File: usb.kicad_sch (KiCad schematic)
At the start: 1 part, among them U2 RTL8211FD-CG

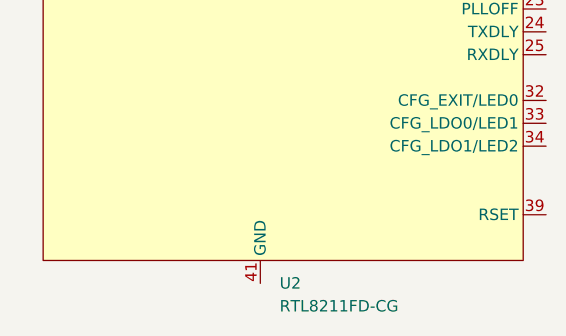
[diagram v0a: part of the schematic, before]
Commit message: Started power circuitry and added more custom schematic symbols
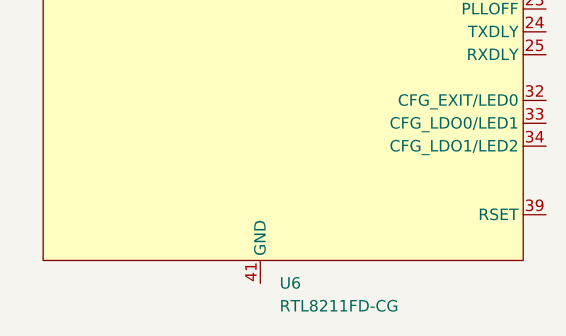
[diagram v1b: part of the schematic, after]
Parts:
- renumbered U2 to U6
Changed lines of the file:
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@@
 		(dnp no)
 		(fields_autoplaced yes)
-		(property "Reference" "U2"
+		(property "Reference" "U6"
 			(at 111.3633 177.8 0)
 			(effects
@@
 		(pin "25"
 		)
+		(instances
+			(project "Leonhart"
+				(path "/b43b7bca-e50d-42ec-8ff0-e0016dfefe0a/0f49ee45-e999-4887-835b-49de9bc4f6ff"
+					(reference "U7")
+					(unit 1)
+				)
+				(path "/b43b7bca-e50d-42ec-8ff0-e0016dfefe0a/5ce8c427-fcc7-46d6-9710-77fc43565e4a"
+					(reference "U8")
+					(unit 1)
+				)
+				(path "/b43b7bca-e50d-42ec-8ff0-e0016dfefe0a/e2459660-886d-4599-a9e6-b9bb7931d0e6"
+					(reference "U6")
+					(unit 1)
+				)
+			)
+		)
 	)

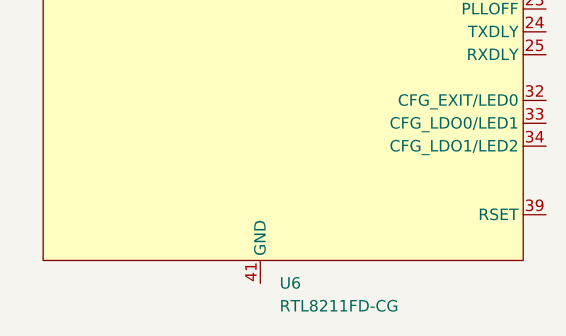
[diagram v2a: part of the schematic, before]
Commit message: Fixed schematic symbol errors
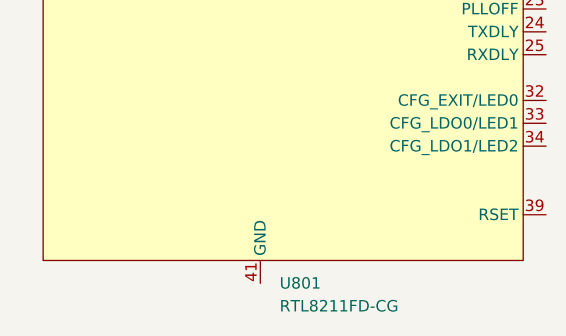
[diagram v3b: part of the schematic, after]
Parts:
- removed U6: RTL8211FD-CG, symbol SoftServicesSymbolLibrary:RTL8211FD-CG
- added U801: RTL8211FD-CG, symbol SoftServicesSymbolLibrary:RTL8211FD-CG
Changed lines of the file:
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@@
 		(dnp no)
 		(fields_autoplaced yes)
-		(property "Reference" "U6"
+		(property "Reference" "U801"
 			(at 111.3633 177.8 0)
 			(effects
@@
 			(project "Leonhart"
 				(path "/b43b7bca-e50d-42ec-8ff0-e0016dfefe0a/e2459660-886d-4599-a9e6-b9bb7931d0e6"
-					(reference "U6")
+					(reference "U801")
 					(unit 1)
 				)

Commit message: Added some net labels and schematic routing
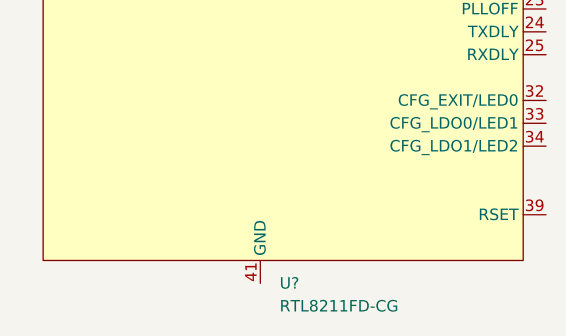
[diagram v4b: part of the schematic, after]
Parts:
- renumbered U801 to U?
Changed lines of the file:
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@@
 		(dnp no)
 		(fields_autoplaced yes)
-		(property "Reference" "U801"
+		(property "Reference" "U?"
 			(at 111.3633 177.8 0)
 			(effects
@@
 			(project "Leonhart"
 				(path "/b43b7bca-e50d-42ec-8ff0-e0016dfefe0a/e2459660-886d-4599-a9e6-b9bb7931d0e6"
-					(reference "U801")
+					(reference "U?")
 					(unit 1)
 				)

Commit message: Worked on schematic for DDR4 memory
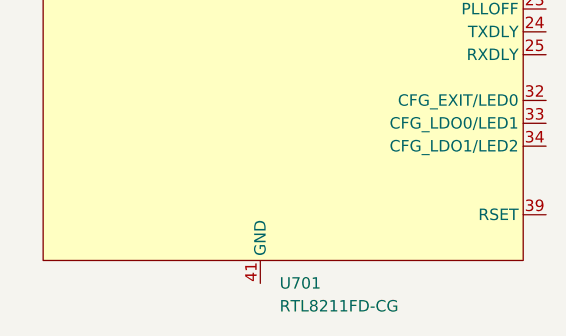
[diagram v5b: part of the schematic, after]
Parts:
- gave numbers to parts that had none: 1
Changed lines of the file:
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@@
 		(dnp no)
 		(fields_autoplaced yes)
-		(property "Reference" "U?"
+		(property "Reference" "U701"
 			(at 111.3633 177.8 0)
 			(effects
@@
 			(project "Leonhart"
 				(path "/b43b7bca-e50d-42ec-8ff0-e0016dfefe0a/e2459660-886d-4599-a9e6-b9bb7931d0e6"
-					(reference "U?")
+					(reference "U701")
 					(unit 1)
 				)

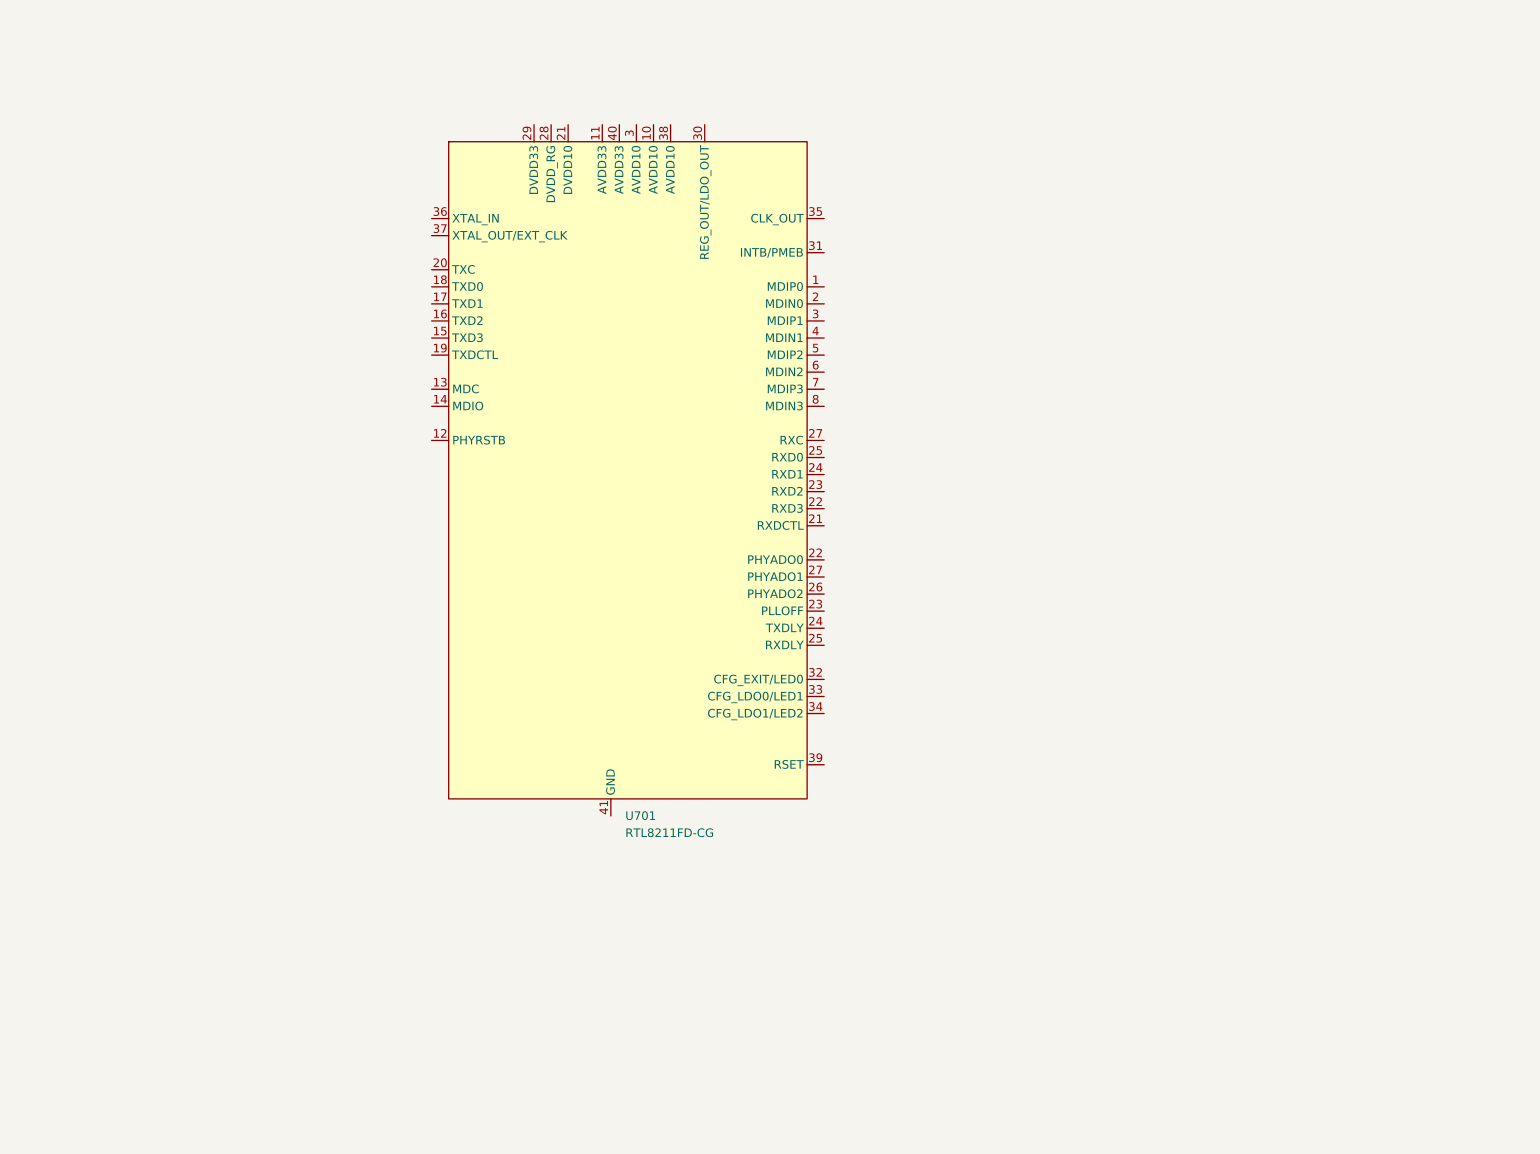
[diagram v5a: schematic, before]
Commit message: Added USB A and USB C to the schematic
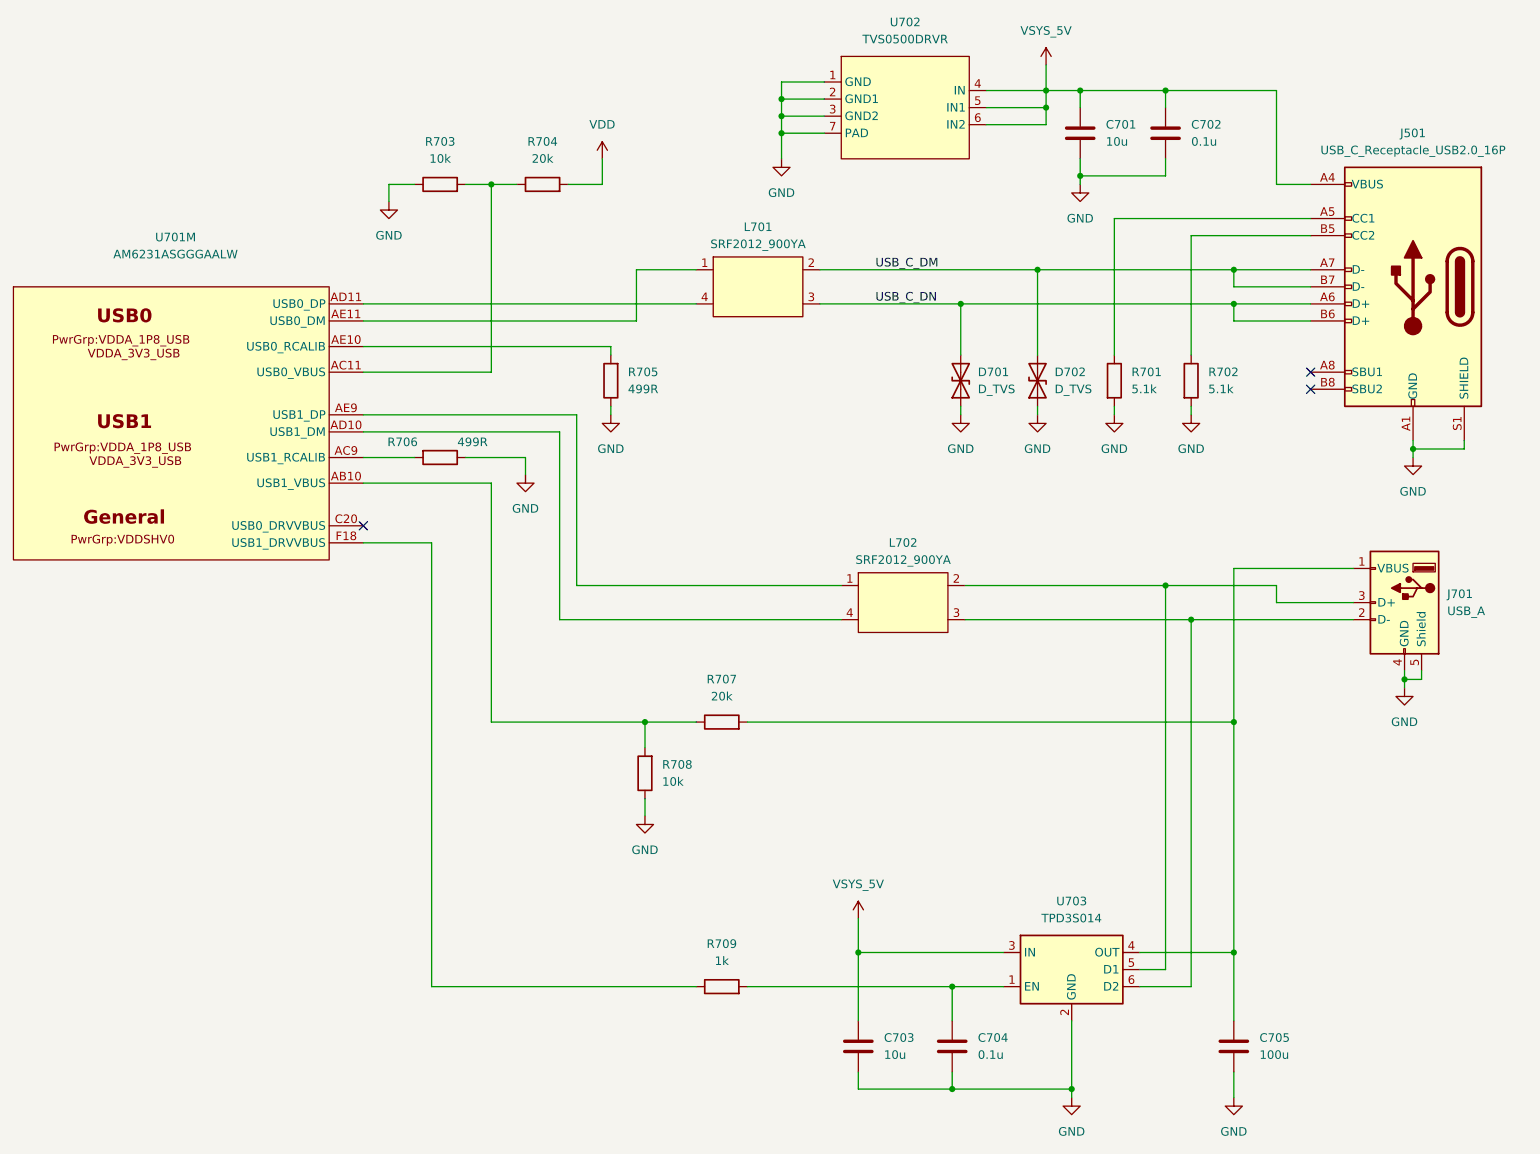
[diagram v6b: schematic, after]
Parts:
- removed U701: RTL8211FD-CG, symbol SoftServicesSymbolLibrary:RTL8211FD-CG
- added C701, C703: 10u, symbol Device:C
- added C702, C704: 0.1u, symbol Device:C
- added C705: 100u, symbol Device:C
- added D701, D702: D_TVS, symbol Device:D_TVS
- added J501: USB_C_Receptacle_USB2.0_16P, symbol Connector:USB_C_Receptacle_USB2.0_16P
- added J701: USB_A, symbol Connector:USB_A
- added L701, L702: SRF2012_900YA, symbol SoftServicesSymbolLibrary:SRF2012_900YA
- added R701, R702: 5.1k, symbol Device:R
- added R703, R708: 10k, symbol Device:R
- added R704, R707: 20k, symbol Device:R
- added R705, R706: 499R, symbol Device:R
- added R709: 1k, symbol Device:R
- added U701: AM6231ASGGGAALW, symbol SoftServicesSymbolLibrary:AM6231ASGGGAALW
- added U702: TVS0500DRVR, symbol SoftServicesSymbolLibrary:TVS0500DRVR
- added U703: TPD3S014, Package_TO_SOT_SMD:SOT-23-6, symbol Power_Protection:TPD3S014
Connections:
- new net: R703.2, R704.1, U701.AC11 (USB0_VBUS)
- new net: C704.1, R709.2, U703.1 (EN)
- new net: R705.2, U701.AE10 (USB0_RCALIB)
- new net: C705.1, J701.1 (VBUS), R707.2, U703.4 (OUT)
- new net: J701.2 (D-), L702.3, U703.6 (D2)
- new net: J701.3 (D+), L702.2, U703.5 (D1)
- new net: J501.B5 (CC2), R702.1
- new net: R706.2, U701.AC9 (USB1_RCALIB)
- new net: J501.A5 (CC1), R701.1
- new net: L702.1, U701.AE9 (USB1_DP)
- new net: L702.4, U701.AD10 (USB1_DM)
- new net: R707.1, R708.2, U701.AB10 (USB1_VBUS)
- new net: R709.1, U701.F18 (USB1_DRVVBUS)
- new net: L701.1, U701.AE11 (USB0_DM)
- new net: L701.4, U701.AD11 (USB0_DP)
- new net GND: C701.2, C702.2, C703.2, C704.2, C705.2, D701.1 (A1), D702.1 (A1), J501.A1 (GND), J501.A12 (GND), J501.B1 (GND), J501.B12 (GND), J501.S1 (SHIELD), J701.4 (GND), J701.5 (Shield), R701.2, R702.2, R703.1, R705.1, R706.1, R708.1, U702.1 (GND), U702.2 (GND1), U702.3 (GND2), U702.7 (PAD), U703.2 (GND)
- new net USB_C_DM: D702.2 (A2), J501.A7 (D-), J501.B7 (D-), L701.2
- new net USB_C_DN: D701.2 (A2), J501.A6 (D+), J501.B6 (D+), L701.3
- new net VDD: R704.2
- new net VSYS_5V: C701.1, C702.1, C703.1, J501.A4 (VBUS), J501.A9 (VBUS), J501.B4 (VBUS), J501.B9 (VBUS), U702.4 (IN), U702.5 (IN1), U702.6 (IN2), U703.3 (IN)
- no-connect marks 0 -> 3
